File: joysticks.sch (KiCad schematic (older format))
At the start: 37 parts, among them CN4 JOY1, CN5 JOY2, U11 74LS125, U17 74AHCT244, U18 74AHCT244

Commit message: Fix joystick buffers ^___^
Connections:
- net GND: now also U17.13 (2A2), U18.13 (2A2); no longer U17.15 (2A1), U18.15 (2A1)
- net 1u: now reaches FB24.1, RP2.2 (R1)
- net 1u: now also U17.8 (1A3); no longer U17.13 (2A2)
- net 1d: now reaches FB25.1, RP2.6 (R5)
- net 1d: now also U17.4 (1A1); no longer U17.2 (1A0)
- net 1r: now reaches FB27.1, RP2.5 (R4)
- net 1r: now also U17.2 (1A0); no longer U17.4 (1A1)
- net 1l: now reaches FB26.1, RP2.3 (R2)
- net 1l: now also U17.6 (1A2); no longer U17.8 (1A3)
- net 1f: now reaches FB28.1, RP2.4 (R3)
- net 1f: now also U17.15 (2A1); no longer U17.6 (1A2)
- net 2u: now reaches FB31.1, RP5.2 (R1)
- net 2u: now also U18.8 (1A3); no longer U18.13 (2A2)
- net 2d: now reaches FB32.1, RP5.6 (R5)
- net 2d: now also U18.4 (1A1); no longer U18.2 (1A0)
- net 2r: now reaches FB34.1, RP5.5 (R4)
- net 2r: now also U18.2 (1A0); no longer U18.4 (1A1)
- net 2l: now reaches FB33.1, RP5.3 (R2)
- net 2l: now also U18.6 (1A2); no longer U18.8 (1A3)
- net 2f: now reaches FB35.1, RP5.4 (R3)
- net 2f: now also U18.15 (2A1); no longer U18.6 (1A2)
- net at U18.12 (1Y3): now also RN2.9 (R5.1); no longer RN2.3 (R2.1)
- net at U18.18 (1Y0): now also RN2.3 (R2.1); no longer RN2.9 (R5.1)
- net at U18.3 (2Y0): no longer RN2.5 (R3.1)
- net at U18.5 (2Y1): now also RN2.5 (R3.1)
- net at U17.12 (1Y3): now also RN1.9 (R5.1); no longer RN1.3 (R2.1)
- net at U17.18 (1Y0): now also RN1.3 (R2.1); no longer RN1.9 (R5.1)
- net at U17.3 (2Y0): no longer RN1.5 (R3.1)
- net at U17.5 (2Y1): now also RN1.5 (R3.1)
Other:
- note added: "The (apparently)\nodd connections\nhere are to\nsimplify routing!"
- note added: "The JD1 and JD2 jumpers are not present\nin the original schematics but I have traced\nthem on my board. They are labeled "D1" and\n"D2", I have renamed them to avoid conflicts\nwith the diodes bearing the same labels.\n\nTheir purpose seems to be able to enable the\njoysticks after passing through the keyboard\ndriver. Since it seems the latter was introduced\nlate in the x264 architecture, mayb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"
- note removed: "The JD1 and JD2 jumpers are not present\nin the original schematics, but I have traced\nthem on my board. They are labeled "D1" and\n"D2", I have renamed them to avoid conflicts\nwith the diodes bearing the same labels.\n\nTheir purpose seems to be able to enable the\njoysticks after passing through the keyboard\ndriver. Since it seems the latter was introduced\nlate in the x264 architecture, may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"
- note removed: "The odd connections here\nare to simplify routing!"
- moved on the sheet: D1, D10, D4, D6, D9, RN1B, RN1E, RN2B, RN2C, RN2E

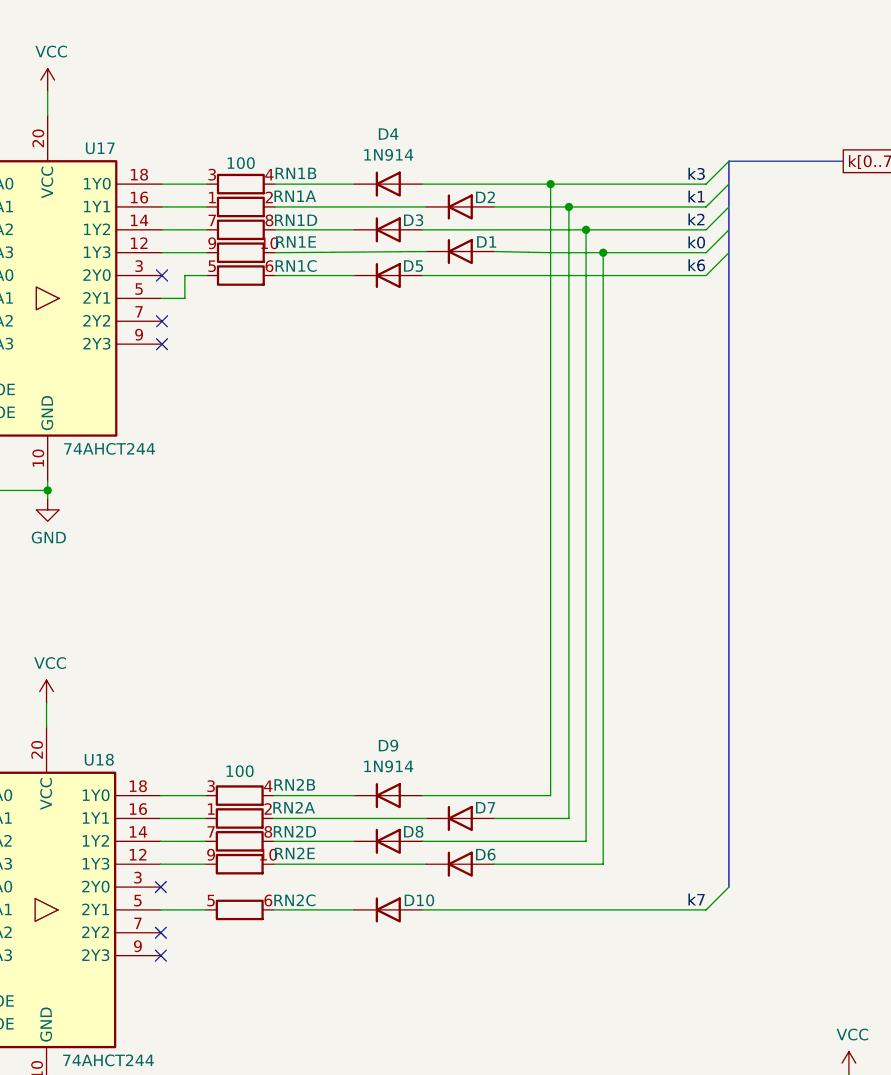
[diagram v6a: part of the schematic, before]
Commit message: Improve power zones
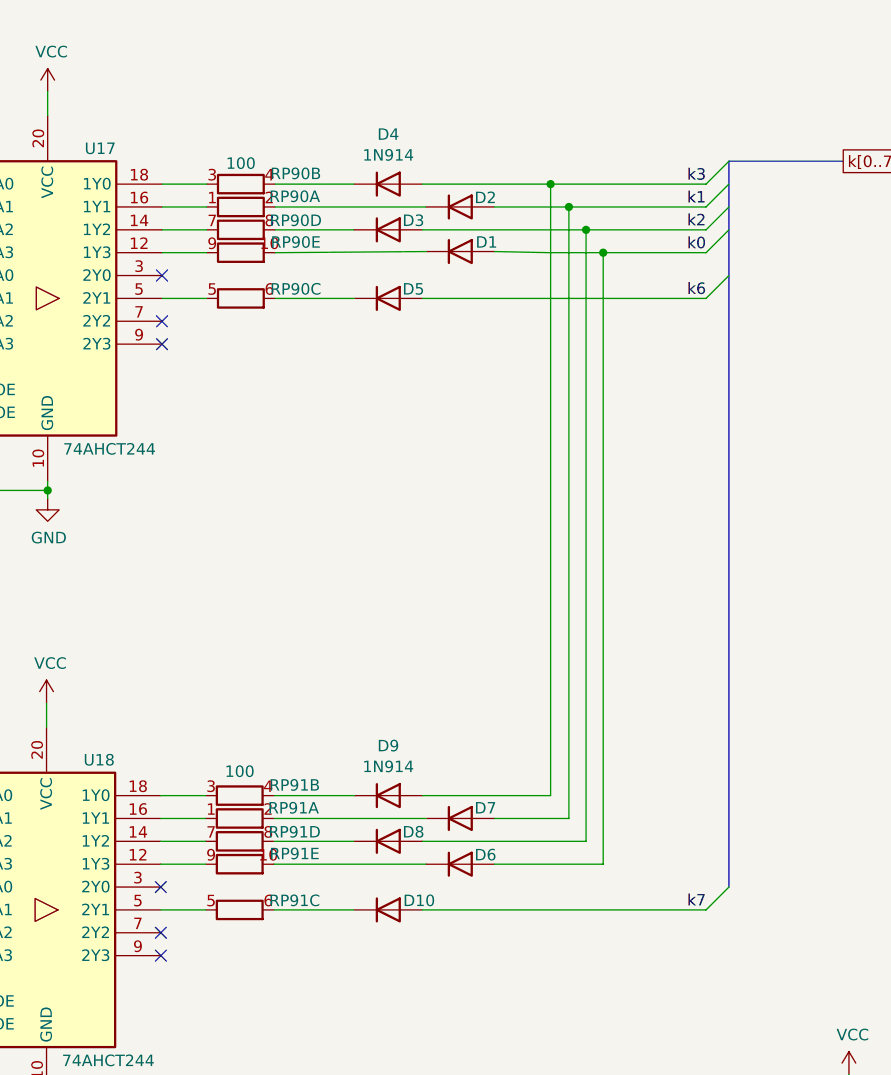
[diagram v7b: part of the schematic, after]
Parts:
- RP2: Notes (none) -> Bussed
- RP90: renamed from RN1; Notes (none) -> Independent
- RP91: renamed from RN2; Notes (none) -> Independent
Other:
- moved on the sheet: D5, RP90C
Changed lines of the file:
@@
 Sheet 11 12
 Title "LittleSixteen"
-Date "2021-11-18"
+Date "2021-11-22"
 Rev "3git"
 Comp "SukkoPera"
@@
 Text Label 9585 4980 2    50   ~ 0
 k7
-Text Label 9585 2205 2    50   ~ 0
+Text Label 9585 2305 2    50   ~ 0
 k6
 Text Label 9585 2005 2    50   ~ 0
@@
 F 2 "Resistor_THT:R_Array_SIP6" V 6105 1280 50  0001 C CNN
 F 3 "http://www.vishay.com/docs/31509/csc.pdf" H 5730 1280 50  0001 C CNN
+F 4 "Bussed" H 5730 1280 50  0001 C CNN "Notes"
 	1    5730 1280
 	1    0    0    -1
@@
 L Diode:1N914 D5
 U 1 1 5E07A0F3
-P 8195 2205
-F 0 "D5" H 8305 2245 50  0000 C CNN
-F 1 "1N914" H 8195 1990 50  0001 C CNN
-F 2 "Diode_THT:D_DO-35_SOD27_P5.08mm_Vertical_KathodeUp" H 8195 2030 50  0001 C CNN
-F 3 "http://www.vishay.com/docs/85622/1n914.pdf" H 8195 2205 50  0001 C CNN
-	1    8195 2205
+P 8195 2305
+F 0 "D5" H 8305 2345 50  0000 C CNN
+F 1 "1N914" H 8195 2090 50  0001 C CNN
+F 2 "Diode_THT:D_DO-35_SOD27_P5.08mm_Vertical_KathodeUp" H 8195 2130 50  0001 C CNN
+F 3 "http://www.vishay.com/docs/85622/1n914.pdf" H 8195 2305 50  0001 C CNN
+	1    8195 2305
 	1    0    0    -1
 $EndComp
@@
 	9585 1805 9685 1705
 Entry Wire Line
-	9585 2205 9685 2105
+	9585 2305 9685 2205
 Entry Wire Line
 	9585 2105 9685 2005
@@
 	3555 4730 3555 4905
 $Comp
-L Device:R_Pack05_SIP_Split RN2
+L Device:R_Pack05_SIP_Split RP91
 U 2 1 61EB4E58
 P 7545 4480
-F 0 "RN2" V 7500 4720 50  0000 C CNN
+F 0 "RP91" V 7500 4720 50  0000 C CNN
 F 1 "100" V 7429 4480 50  0001 C CNN
 F 2 "Resistor_THT:R_Array_SIP10" V 7465 4480 50  0001 C CNN
 F 3 "http://www.vishay.com/docs/31509/csc.pdf" H 7545 4480 50  0001 C CNN
+F 4 "Independent" H 7545 4480 50  0001 C CNN "Notes"
 	2    7545 4480
 	0    1    1    0
 $EndComp
 $Comp
-L Device:R_Pack05_SIP_Split RN2
+L Device:R_Pack05_SIP_Split RP91
 U 3 1 61EB627F
 P 7545 4980
-F 0 "RN2" V 7505 5220 50  0000 C CNN
+F 0 "RP91" V 7505 5220 50  0000 C CNN
 F 1 "100" V 7429 4980 50  0001 C CNN
 F 2 "Resistor_THT:R_Array_SIP10" V 7465 4980 50  0001 C CNN
 F 3 "http://www.vishay.com/docs/31509/csc.pdf" H 7545 4980 50  0001 C CNN
+F 4 "Independent" H 7545 4980 50  0001 C CNN "Notes"
 	3    7545 4980
 	0    1    1    0
 $EndComp
 $Comp
-L Device:R_Pack05_SIP_Split RN2
+L Device:R_Pack05_SIP_Split RP91
 U 4 1 61EB730F
 P 7545 4680
-F 0 "RN2" V 7505 4920 50  0000 C CNN
+F 0 "RP91" V 7505 4920 50  0000 C CNN
 F 1 "100" V 7429 4680 50  0001 C CNN
 F 2 "Resistor_THT:R_Array_SIP10" V 7465 4680 50  0001 C CNN
 F 3 "http://www.vishay.com/docs/31509/csc.pdf" H 7545 4680 50  0001 C CNN
+F 4 "Independent" H 7545 4680 50  0001 C CNN "Notes"
 	4    7545 4680
 	0    1    1    0
 $EndComp
 $Comp
-L Device:R_Pack05_SIP_Split RN2
+L Device:R_Pack05_SIP_Split RP91
 U 5 1 61EB849F
 P 7545 4780
-F 0 "RN2" V 7500 5020 50  0000 C CNN
+F 0 "RP91" V 7500 5020 50  0000 C CNN
 F 1 "100" V 7429 4780 50  0001 C CNN
 F 2 "Resistor_THT:R_Array_SIP10" V 7465 4780 50  0001 C CNN
 F 3 "http://www.vishay.com/docs/31509/csc.pdf" H 7545 4780 50  0001 C CNN
+F 4 "Independent" H 7545 4780 50  0001 C CNN "Notes"
 	5    7545 4780
 	0    1    1    0
@@
 $EndComp
 $Comp
-L Device:R_Pack05_SIP_Split RN1
+L Device:R_Pack05_SIP_Split RP90
 U 1 1 61FC7C55
 P 7550 1905
-F 0 "RN1" V 7505 2140 50  0000 C CNN
+F 0 "RP90" V 7505 2140 50  0000 C CNN
 F 1 "100" V 7360 1905 50  0000 C CNN
 F 2 "Resistor_THT:R_Array_SIP10" V 7470 1905 50  0001 C CNN
 F 3 "http://www.vishay.com/docs/31509/csc.pdf" H 7550 1905 50  0001 C CNN
+F 4 "Independent" H 7550 1905 50  0001 C CNN "Notes"
 	1    7550 1905
 	0    1    1    0
@@
 	5265 1905 5930 1905
 Wire Wire Line
-	7700 2205 8045 2205
+	7700 2305 8045 2305
 $Comp
 L Diode:1N914 D3
@@
 $EndComp
 Connection ~ 5530 4480
-$Comp
-L Device:R_Pack05_SIP_Split RN2
-U 1 1 61EB0CF8
-P 7545 4580
-F 0 "RN2" V 7500 4815 50  0000 C CNN
-F 1 "100" V 7340 4580 50  0000 C CNN
-F 2 "Resistor_THT:R_Array_SIP10" V 7465 4580 50  0001 C CNN
-F 3 "http://www.vishay.com/docs/31509/csc.pdf" H 7545 4580 50  0001 C CNN
-	1    7545 4580
-	0    1    1    0
-$EndComp
 Wire Wire Line
 	7700 2005 8045 2005
 $Comp
-L Device:R_Pack05_SIP_Split RN1
+L Device:R_Pack05_SIP_Split RP90
 U 3 1 61FC7C69
-P 7550 2205
-F 0 "RN1" V 7510 2445 50  0000 C CNN
-F 1 "100" V 7434 2205 50  0001 C CNN
-F 2 "Resistor_THT:R_Array_SIP10" V 7470 2205 50  0001 C CNN
-F 3 "http://www.vishay.com/docs/31509/csc.pdf" H 7550 2205 50  0001 C CNN
-	3    7550 2205
-	0    1    1    0
-$EndComp
-$Comp
-L Device:R_Pack05_SIP_Split RN1
+P 7550 2305
+F 0 "RP90" V 7510 2545 50  0000 C CNN
+F 1 "100" V 7434 2305 50  0001 C CNN
+F 2 "Resistor_THT:R_Array_SIP10" V 7470 2305 50  0001 C CNN
+F 3 "http://www.vishay.com/docs/31509/csc.pdf" H 7550 2305 50  0001 C CNN
+F 4 "Independent" H 7550 2305 50  0001 C CNN "Notes"
+	3    7550 2305
+	0    1    1    0
+$EndComp
+$Comp
+L Device:R_Pack05_SIP_Split RP90
 U 4 1 61FC7C73
 P 7550 2005
-F 0 "RN1" V 7510 2245 50  0000 C CNN
+F 0 "RP90" V 7510 2245 50  0000 C CNN
 F 1 "100" V 7434 2005 50  0001 C CNN
 F 2 "Resistor_THT:R_Array_SIP10" V 7470 2005 50  0001 C CNN
 F 3 "http://www.vishay.com/docs/31509/csc.pdf" H 7550 2005 50  0001 C CNN
+F 4 "Independent" H 7550 2005 50  0001 C CNN "Notes"
 	4    7550 2005
 	0    1    1    0
@@
 	5730 2205 5730 2305
 Connection ~ 5730 2205
-Wire Wire Line
-	7305 2205 7400 2205
 NoConn ~ 7205 2205
 Wire Wire Line
@@
 Wire Wire Line
 	5730 2305 6205 2305
-Wire Wire Line
-	7205 2305 7305 2305
-Wire Wire Line
-	7305 2305 7305 2205
 NoConn ~ 7205 2405
 Wire Wire Line
@@
 	7205 2105 7400 2105
 $Comp
-L Device:R_Pack05_SIP_Split RN1
+L Device:R_Pack05_SIP_Split RP90
 U 5 1 61FC7C7D
 P 7550 2105
-F 0 "RN1" V 7505 2345 50  0000 C CNN
+F 0 "RP90" V 7505 2345 50  0000 C CNN
 F 1 "100" V 7434 2105 50  0001 C CNN
 F 2 "Resistor_THT:R_Array_SIP10" V 7470 2105 50  0001 C CNN
 F 3 "http://www.vishay.com/docs/31509/csc.pdf" H 7550 2105 50  0001 C CNN
+F 4 "Independent" H 7550 2105 50  0001 C CNN "Notes"
 	5    7550 2105
 	0    1    1    0
@@
 	7700 1805 8045 1805
 $Comp
-L Device:R_Pack05_SIP_Split RN1
+L Device:R_Pack05_SIP_Split RP90
 U 2 1 61FC7C5F
 P 7550 1805
-F 0 "RN1" V 7505 2045 50  0000 C CNN
+F 0 "RP90" V 7505 2045 50  0000 C CNN
 F 1 "100" V 7434 1805 50  0001 C CNN
 F 2 "Resistor_THT:R_Array_SIP10" V 7470 1805 50  0001 C CNN
 F 3 "http://www.vishay.com/docs/31509/csc.pdf" H 7550 1805 50  0001 C CNN
+F 4 "Independent" H 7550 1805 50  0001 C CNN "Notes"
 	2    7550 1805
 	0    1    1    0
 $EndComp
 Wire Wire Line
-	8345 2205 9585 2205
+	8345 2305 9585 2305
 Wire Wire Line
 	5830 1725 6100 1725
@@
 Wire Wire Line
 	8985 1905 8985 4580
+$Comp
+L Device:R_Pack05_SIP_Split RP91
+U 1 1 61EB0CF8
+P 7545 4580
+F 0 "RP91" V 7500 4815 50  0000 C CNN
+F 1 "100" V 7340 4580 50  0000 C CNN
+F 2 "Resistor_THT:R_Array_SIP10" V 7465 4580 50  0001 C CNN
+F 3 "http://www.vishay.com/docs/31509/csc.pdf" H 7545 4580 50  0001 C CNN
+F 4 "Independent" H 7545 4580 50  0001 C CNN "Notes"
+	1    7545 4580
+	0    1    1    0
+$EndComp
+Wire Wire Line
+	7205 2305 7400 2305
 Wire Bus Line
 	9685 1705 9685 4880

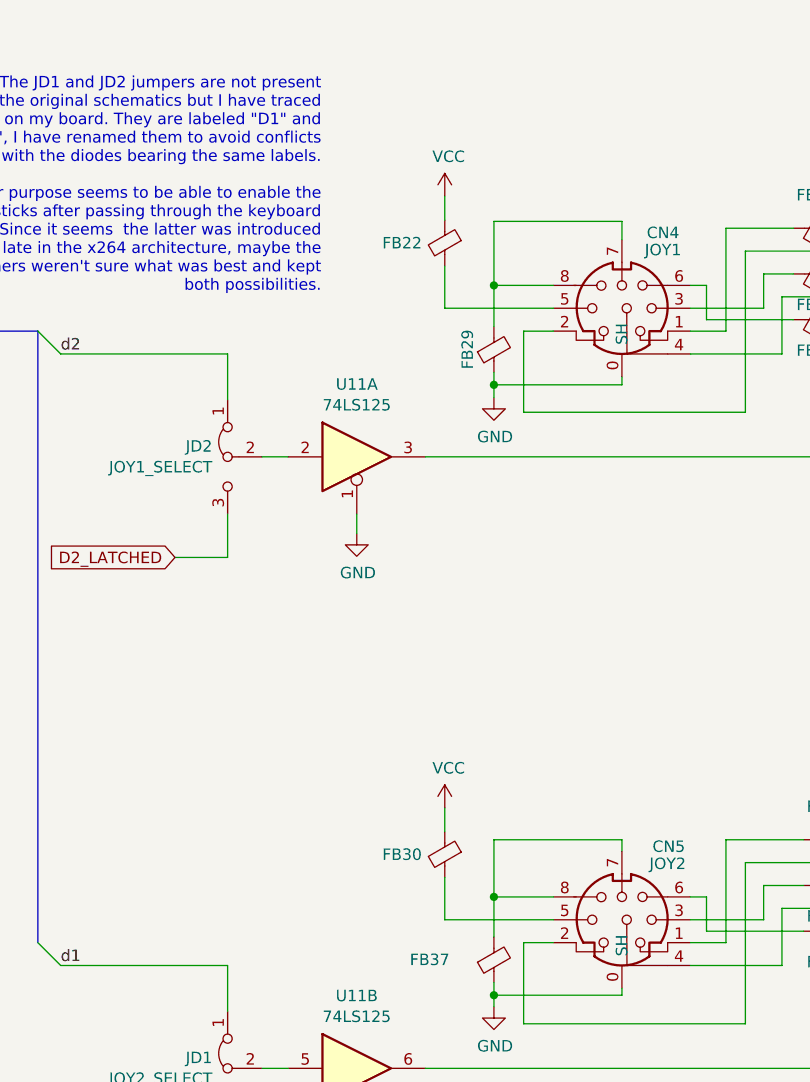
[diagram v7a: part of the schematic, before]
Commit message: Add current-limiting resistors on joystick ports and start working on silkscreen
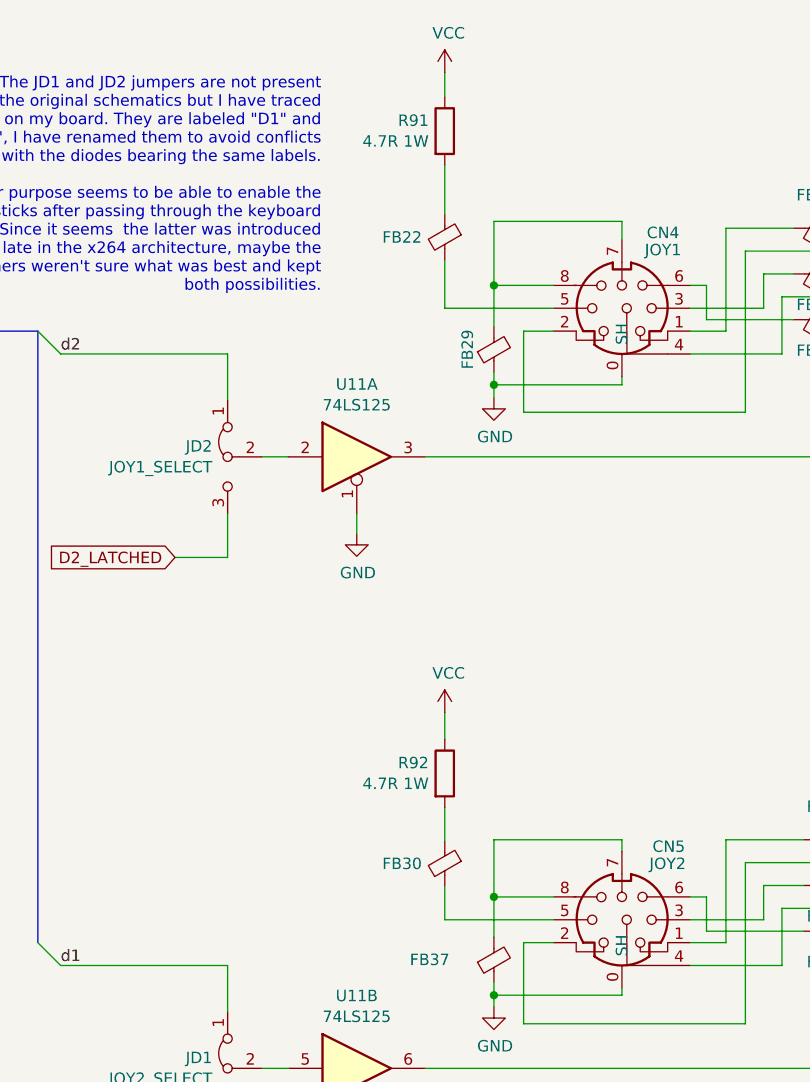
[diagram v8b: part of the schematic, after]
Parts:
- added R91, R92: 4.7R 1W, Resistor_THT:R_Axial_DIN0414_L11.9mm_D4.5mm_P5.08mm_Vertical, symbol Device:R
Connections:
- net VCC: now also R91.1, R92.1; no longer FB22.1, FB30.1
- new net: FB22.1, R91.2
- new net: FB30.1, R92.2
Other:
- moved on the sheet: FB22, FB30
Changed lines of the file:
@@
 	3340 4830 3815 4830
 Wire Wire Line
-	3340 4645 3340 4830
-Wire Wire Line
-	3340 4340 3340 4445
+	3340 4340 3340 4485
 $Comp
 L Device:Ferrite_Bead_Small FB30
 U 1 1 5E19A89F
-P 3340 4545
-F 0 "FB30" H 3440 4545 50  0000 L CNN
-F 1 "Ferrite_Bead_Small" V 3194 4545 50  0001 C CNN
-F 2 "LittleSixteen:Ferrite" V 3270 4545 50  0001 C CNN
-F 3 "~" H 3340 4545 50  0001 C CNN
-	1    3340 4545
+P 3340 4585
+F 0 "FB30" H 3440 4585 50  0000 L CNN
+F 1 "Ferrite_Bead_Small" V 3194 4585 50  0001 C CNN
+F 2 "LittleSixteen:Ferrite" V 3270 4585 50  0001 C CNN
+F 3 "~" H 3340 4585 50  0001 C CNN
+	1    3340 4585
 	-1   0    0    -1
 $EndComp
@@
 L power:VCC #PWR0111
 U 1 1 5E19A85B
-P 3340 4340
-F 0 "#PWR0111" H 3340 4190 50  0001 C CNN
-F 1 "VCC" H 3357 4513 50  0000 C CNN
-F 2 "" H 3340 4340 50  0001 C CNN
-F 3 "" H 3340 4340 50  0001 C CNN
-	1    3340 4340
+P 3340 3925
+F 0 "#PWR0111" H 3340 3775 50  0001 C CNN
+F 1 "VCC" H 3357 4098 50  0000 C CNN
+F 2 "" H 3340 3925 50  0001 C CNN
+F 3 "" H 3340 3925 50  0001 C CNN
+	1    3340 3925
 	1    0    0    -1
 $EndComp
@@
 	3340 2155 3815 2155
 Wire Wire Line
-	3340 1970 3340 2155
-Wire Wire Line
-	3340 1665 3340 1770
+	3340 1530 3340 1745
+Wire Wire Line
+	3340 1125 3340 1230
 $Comp
 L Device:Ferrite_Bead_Small FB22
 U 1 1 5E094DB1
-P 3340 1870
-F 0 "FB22" H 3440 1870 50  0000 L CNN
-F 1 "Ferrite_Bead_Small" V 3194 1870 50  0001 C CNN
-F 2 "LittleSixteen:Ferrite" V 3270 1870 50  0001 C CNN
-F 3 "~" H 3340 1870 50  0001 C CNN
-	1    3340 1870
+P 3340 1845
+F 0 "FB22" H 3440 1845 50  0000 L CNN
+F 1 "Ferrite_Bead_Small" V 3194 1845 50  0001 C CNN
+F 2 "LittleSixteen:Ferrite" V 3270 1845 50  0001 C CNN
+F 3 "~" H 3340 1845 50  0001 C CNN
+	1    3340 1845
 	-1   0    0    -1
 $EndComp
@@
 L power:VCC #PWR0108
 U 1 1 5E057834
-P 3340 1665
-F 0 "#PWR0108" H 3340 1515 50  0001 C CNN
-F 1 "VCC" H 3357 1838 50  0000 C CNN
-F 2 "" H 3340 1665 50  0001 C CNN
-F 3 "" H 3340 1665 50  0001 C CNN
-	1    3340 1665
+P 3340 1125
+F 0 "#PWR0108" H 3340 975 50  0001 C CNN
+F 1 "VCC" H 3357 1298 50  0000 C CNN
+F 2 "" H 3340 1125 50  0001 C CNN
+F 3 "" H 3340 1125 50  0001 C CNN
+	1    3340 1125
 	1    0    0    -1
 $EndComp
@@
 Wire Wire Line
 	7205 2305 7400 2305
+$Comp
+L Device:R R91
+U 1 1 62AFB1A5
+P 3340 1380
+F 0 "R91" H 3270 1426 50  0000 R CNN
+F 1 "4.7R 1W" H 3270 1335 50  0000 R CNN
+F 2 "Resistor_THT:R_Axial_DIN0414_L11.9mm_D4.5mm_P5.08mm_Vertical" V 3270 1380 50  0001 C CNN
+F 3 "~" H 3340 1380 50  0001 C CNN
+	1    3340 1380
+	1    0    0    -1
+$EndComp
+Wire Wire Line
+	3340 1945 3340 2155
+$Comp
+L Device:R R92
+U 1 1 62B0FE1B
+P 3340 4190
+F 0 "R92" H 3270 4236 50  0000 R CNN
+F 1 "4.7R 1W" H 3270 4145 50  0000 R CNN
+F 2 "Resistor_THT:R_Axial_DIN0414_L11.9mm_D4.5mm_P5.08mm_Vertical" V 3270 4190 50  0001 C CNN
+F 3 "~" H 3340 4190 50  0001 C CNN
+	1    3340 4190
+	1    0    0    -1
+$EndComp
+Wire Wire Line
+	3340 4685 3340 4830
+Wire Wire Line
+	3340 4040 3340 3925
 Wire Bus Line
 	9685 1705 9685 4880
